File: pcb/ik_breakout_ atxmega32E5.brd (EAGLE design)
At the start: 41.3 x 20.3 mm, 31 parts, among them IC1 FT230XS, J1 AVR_SPI_PRG_62X3_LOCK, U1 MIC5219 3.3V

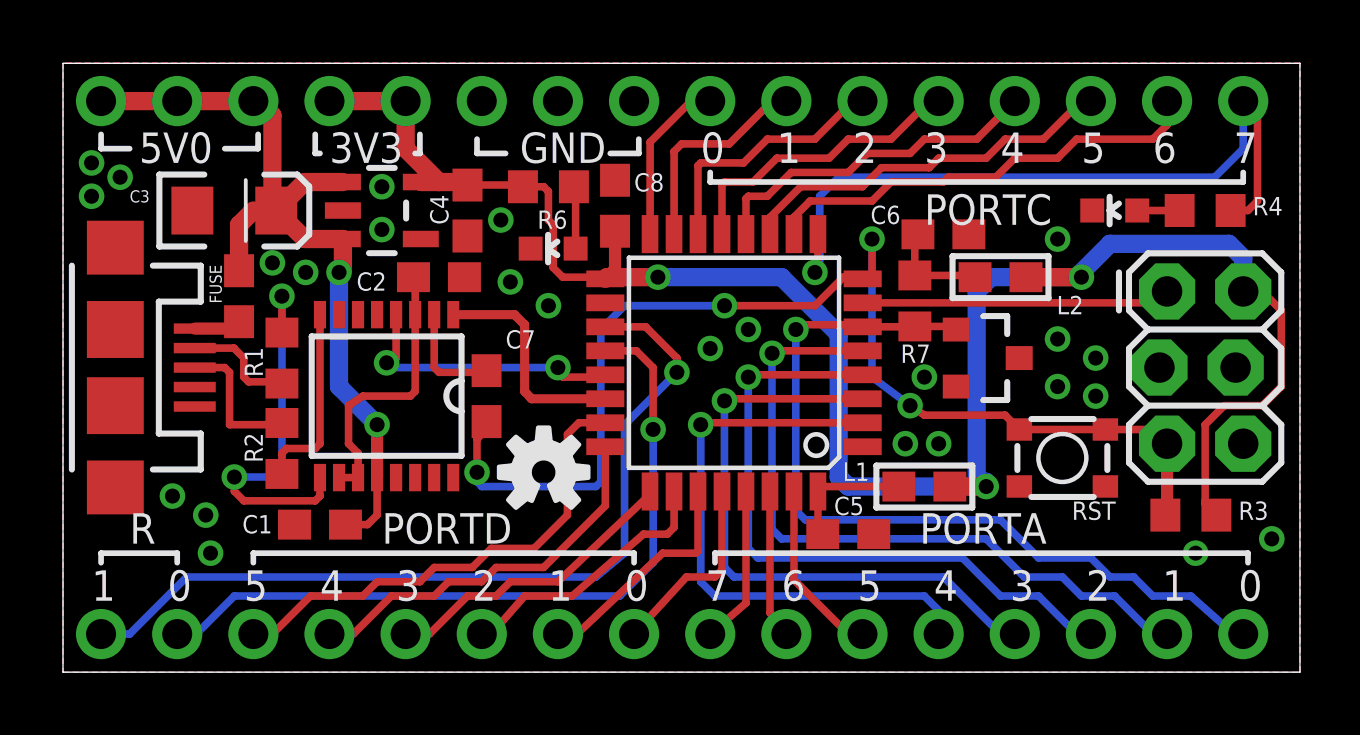
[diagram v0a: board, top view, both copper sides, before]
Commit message: oops. committed from /pcb/fab/gerbers folder.
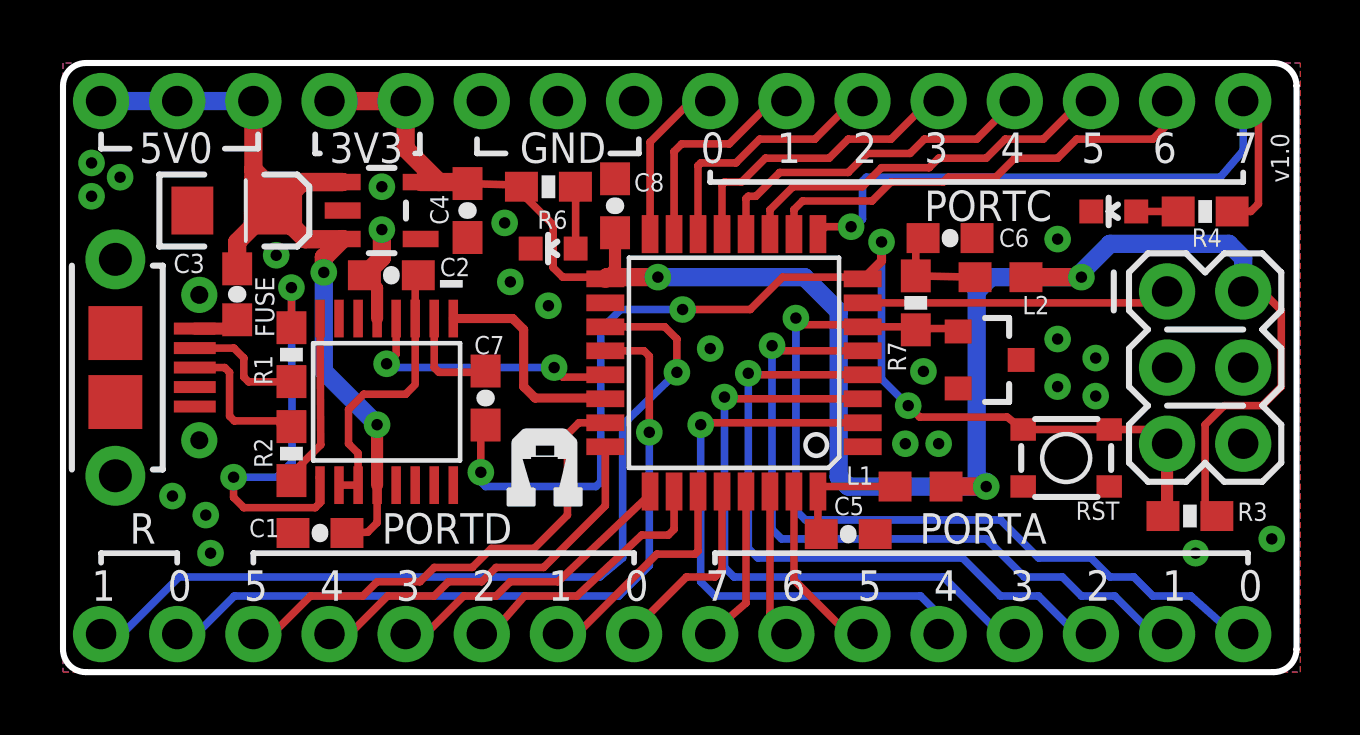
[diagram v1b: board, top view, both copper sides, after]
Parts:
- removed JP6, JP7, JP8, JP9: (no value), microbuilder:1X08_ROUND
- removed LED3: (no value), SparkFun-LED:LED-0603
- removed U$1: IHSAN_XMEGA_E5, SparkFun-DigitalIC_ihsan:TQFP32-08
- removed U$2: IHSAN_LM4040, SparkFun-DigitalIC_ihsan:SOT23-3
- added IC2: ATXMEGA32E5, Ai_IC:TQFP32-08
- added JP1, JP2, JP3, JP4: 1X08NOFIRST, Ai_Connectors:1X08-NOFIRST
- added LED1: (no value), Ai_LED:LED-0603
- added U$3: AI-LOGOXS, Ai_Miscellany:AI-LOGO-XS
- added U2: IHSAN_LM4040, SparkFun-DigitalIC_ihsan:SOT23-3
- C1, C2, C5, C6, C7: value .1 -> 0.1uF; device rcl:C0603 -> Ai_Passives:CAP-0603
- C3: device SparkFun-Capacitors:EIA3216 -> Ai_Passives:CAP-POL-EIA3216
- C4, C8: value 4.7 uF -> 4.7uF; device rcl:C0603 -> Ai_Passives:CAP-0603
- FUSE: device SparkFun-Passives:0603 -> Ai_Passives:FB-0603
- IC1: value FT230XS -> FT230X; device ftdichip:SSOP16 -> Ai_IC:SSOP-16-FTDI
- J1: value AVR_SPI_PRG_62X3_LOCK -> 2X03; device SparkFun-Connectors:2X3_LOCK -> Ai_Connectors:2X03
- L1, L2: device microbuilder:0603 -> Ai_Passives:IND-0603
- LED2: device SparkFun-LED:LED-0603 -> Ai_LED:LED-0603
- R1, R2, R3, R4, R6, R7: device rcl:R0603 -> Ai_Passives:RES-0603
- U1: value MIC5219 3.3V -> MIC5219-3.3; device SparkFun-PowerIC:SOT23-5 -> Ai_Power:SOT23-5
- USB1: value USBMICROB-SMD -> USBMICROB-TH; device Ai_Connectors:USB-MICROB-SMD -> Ai_Connectors:USB-MICROB-TH
- moved LOGO1 9.09 mm to (22.4, 13.2), flipped to the bottom
- moved J1 2.84 mm to (38.1, 10.2)
- moved C2 1.59 mm to (11.0, 13.2), turned to 180 degrees
- moved R2 0.36 mm to (7.62, 7.29)
- moved R1 0.34 mm to (7.62, 10.6)
- moved C1 0.28 mm to (8.57, 4.64)
- moved C6 0.26 mm to (29.6, 14.5)
- moved IC1 0.19 mm to (10.8, 9.02), turned to 180 degrees
- moved RST 0.13 mm to (33.5, 7.14)
- moved L1 0.13 mm to (28.6, 6.19)
- moved FUSE 0.09 mm to (5.81, 12.6), turned to 90 degrees
- moved C7 0.07 mm to (14.1, 9.14)
- moved R7 0.07 mm to (28.4, 12.3)
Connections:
- net /RTS renamed !RTS
- removed net 5V0: C1.1, C3.A, FUSE.1, IC1.12, JP9.1, JP9.2, JP9.3, U1.1, U1.3
- removed net N$10: FUSE.2, USB1.VBUS
- new net 5V: C1.1, C3.A, FUSE.2, IC1.12, JP4.1, JP4.2, JP4.3, U1.1, U1.3
- new net VBUS: FUSE.1, USB1.VBUS
- net 3V3: now also IC2.17, JP4.4, JP4.5; no longer JP9.4, JP9.5, U$1.17
- net AVCC: now also IC2.32; no longer U$1.32
- net FT_RX: now also IC2.21; no longer U$1.21
- net FT_TX: now also IC2.22; no longer U$1.22
- net GND: now also IC2.1, IC2.18, JP4.6, JP4.7, JP4.8, LED1.C, U2.2; no longer JP9.6, JP9.7, JP9.8, LED3.C, U$1.1, U$1.18, U$2.2
- net N$8: now also LED1.A; no longer LED3.A
- net PA0: now also IC2.6, JP2.1, U2.1; no longer JP8.1, U$1.6, U$2.1
- net PA1: now also IC2.5, JP2.2; no longer JP8.2, U$1.5
- net PA2: now also IC2.4, JP2.3; no longer JP8.3, U$1.4
- net PA3: now also IC2.3, JP2.4; no longer JP8.4, U$1.3
- net PA4: now also IC2.2, JP2.5; no longer JP8.5, U$1.2
- net PA5: now also IC2.31, JP2.6; no longer JP8.6, U$1.31
- net PA6: now also IC2.30, JP2.7; no longer JP8.7, U$1.30
- net PA7: now also IC2.29, JP2.8; no longer JP8.8, U$1.29
- net PC0: now also IC2.16, JP3.1; no longer JP6.1, U$1.16
- net PC1: now also IC2.15, JP3.2; no longer JP6.2, U$1.15
- net PC2: now also IC2.14, JP3.3; no longer JP6.3, U$1.14
- net PC3: now also IC2.13, JP3.4; no longer JP6.4, U$1.13
- net PC4: now also IC2.12, JP3.5; no longer JP6.5, U$1.12
- net PC5: now also IC2.11, JP3.6; no longer JP6.6, U$1.11
- net PC6: now also IC2.10, JP3.7; no longer JP6.7, U$1.10
- net PC7: now also IC2.9, JP3.8; no longer JP6.8, U$1.9
- net PD0: now also IC2.28, JP1.1; no longer JP7.1, U$1.28
- net PD1: now also IC2.27, JP1.2; no longer JP7.2, U$1.27
- net PD2: now also IC2.26, JP1.3; no longer JP7.3, U$1.26
- net PD3: now also IC2.25, JP1.4; no longer JP7.4, U$1.25
- net PD4: now also IC2.24, JP1.5; no longer JP7.5, U$1.24
- net PD5: now also IC2.23, JP1.6; no longer JP7.6, U$1.23
- net PDI_C: now also IC2.8; no longer U$1.8
- net PDI_D: now also IC2.7; no longer U$1.7
- net PR0: now also IC2.20, JP1.7; no longer JP7.7, U$1.20
- net PR1: now also IC2.19, JP1.8; no longer JP7.8, U$1.19
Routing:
- net 5V: track 0.00 -> 31.2 mm, vias 0 -> 2
- net 5V0: track 28.3 -> 0.00 mm, vias 2 -> 0
- net GND: track 0.00 -> 3.38 mm, vias 25 -> 23
- net PC7: track 24.9 -> 22.4 mm
- net N$10: track 1.65 -> 0.00 mm
- net VBUS: track 0.00 -> 1.54 mm
- net D-: track 12.9 -> 13.9 mm
- net PDI_C: track 40.4 -> 39.7 mm
- net D+: track 6.40 -> 5.81 mm
- net PA0: track 28.1 -> 28.7 mm
- net N$2: track 4.74 -> 5.27 mm
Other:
- board size 41.3 x 20.3 mm -> 41.1 x 20.3 mm
- board text added: "ATxmega32E5"
- board text added: "Ihsan Kehribar"
- board text added: "v1.0"
- board text added: "www.acrobotic.com"
- board text removed: "<ihsan@kehribar.me> - 2014"
- board text removed: "Xmega E5"
- board text removed: "v0.4"

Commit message: changed LM4040 to include part on Ai_Power library
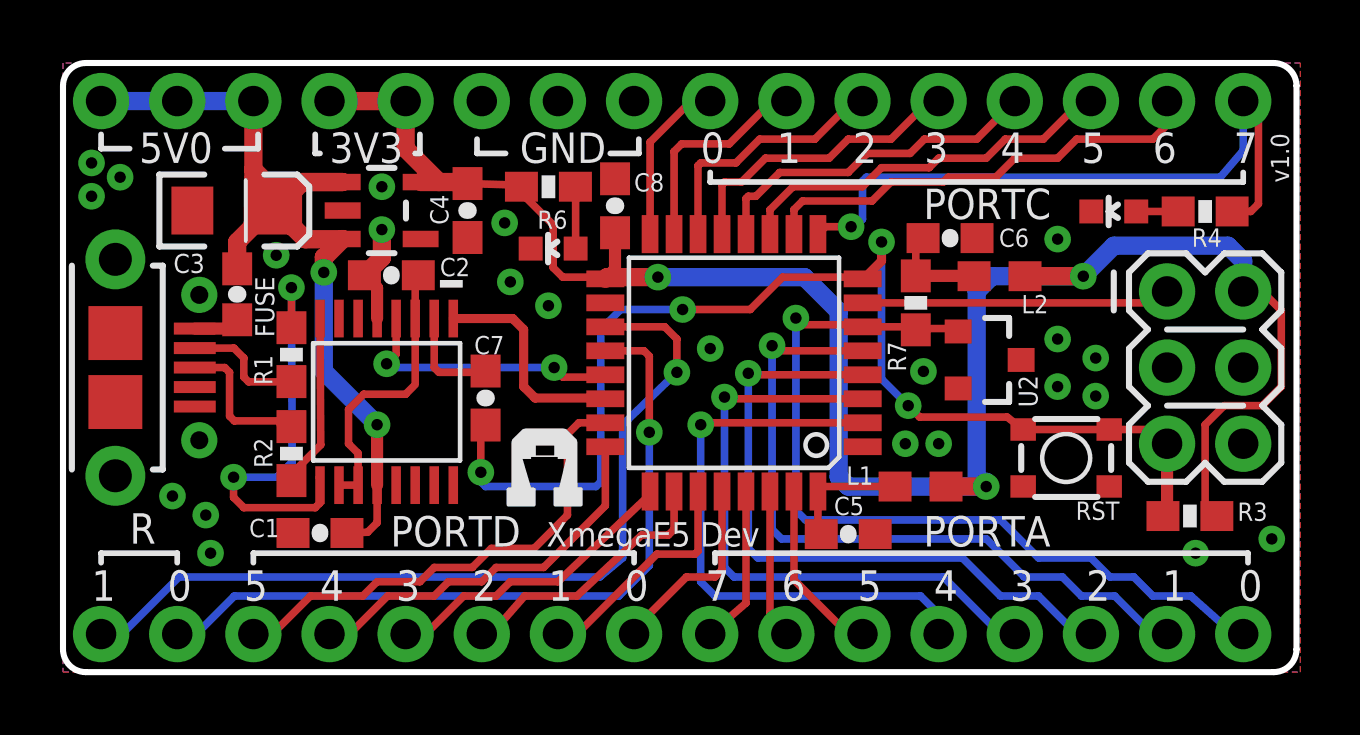
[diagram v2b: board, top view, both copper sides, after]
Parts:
- U2: value IHSAN_LM4040 -> LM4040; device SparkFun-DigitalIC_ihsan:SOT23-3 -> Ai_Power:SOT23-3
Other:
- board text added: "XmegaE5 Dev"
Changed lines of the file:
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@@
 <setting verticaltext="up"/>
 </settings>
-<grid distance="10" unitdist="mil" unit="mil" style="lines" multiple="1" display="yes" altdistance="0.025" altunitdist="inch" altunit="inch"/>
+<grid distance="5" unitdist="mil" unit="mil" style="lines" multiple="1" display="yes" altdistance="0.025" altunitdist="inch" altunit="inch"/>
 <layers>
 <layer number="1" name="Top" color="4" fill="1" visible="yes" active="yes"/>
@@
 <layer number="45" name="Holes" color="7" fill="1" visible="no" active="yes"/>
 <layer number="46" name="Milling" color="3" fill="1" visible="no" active="yes"/>
-<layer number="47" name="Measures" color="7" fill="1" visible="no" active="yes"/>
-<layer number="48" name="Document" color="7" fill="1" visible="no" active="yes"/>
-<layer number="49" name="Reference" color="7" fill="1" visible="no" active="yes"/>
+<layer number="47" name="Measures" color="7" fill="1" visible="yes" active="yes"/>
+<layer number="48" name="Document" color="7" fill="1" visible="yes" active="yes"/>
+<layer number="49" name="Reference" color="7" fill="1" visible="yes" active="yes"/>
 <layer number="50" name="dxf" color="7" fill="1" visible="no" active="no"/>
 <layer number="51" name="tDocu" color="7" fill="1" visible="no" active="yes"/>
@@
 <text x="16.1925" y="2.38125" size="1.016" layer="21" font="vector" ratio="15">1</text>
 <text x="18.7325" y="2.38125" size="1.016" layer="21" font="vector" ratio="15">0</text>
-<text x="10.63625" y="4.28625" size="1.016" layer="21" font="vector" ratio="15">PORTD</text>
+<text x="10.922" y="4.191" size="1.016" layer="21" font="vector" ratio="15">PORTD</text>
 <wire x1="21.74875" y1="3.65125" x2="21.74875" y2="3.96875" width="0.1905" layer="21"/>
 <wire x1="21.74875" y1="3.96875" x2="39.52875" y2="3.96875" width="0.1905" layer="21"/>
@@
 <text x="36.67125" y="2.38125" size="1.016" layer="21" font="vector" ratio="15">1</text>
 <text x="39.21125" y="2.38125" size="1.016" layer="21" font="vector" ratio="15">0</text>
-<text x="28.575" y="4.28625" size="1.016" layer="21" font="vector" ratio="15">PORTA</text>
+<text x="28.702" y="4.191" size="1.016" layer="21" font="vector" ratio="15">PORTA</text>
 <wire x1="39.37" y1="16.66875" x2="39.37" y2="16.35125" width="0.1905" layer="21"/>
 <wire x1="39.37" y1="16.35125" x2="21.59" y2="16.35125" width="0.1905" layer="21"/>
@@
 <text x="23.8125" y="16.98625" size="1.016" layer="21" font="vector" ratio="15">1</text>
 <text x="21.2725" y="16.98625" size="1.016" layer="21" font="vector" ratio="15">0</text>
-<text x="28.73375" y="15.0495" size="1.016" layer="21" font="vector" ratio="15">PORTC</text>
+<text x="28.702" y="15.113" size="1.016" layer="21" font="vector" ratio="15">PORTC</text>
 <text x="2.54" y="16.98625" size="1.016" layer="21" font="vector" ratio="15">5V0</text>
 <text x="8.89" y="16.98625" size="1.016" layer="21" font="vector" ratio="15">3V3</text>
@@
 <text x="14.224" y="5.55625" size="1.016" layer="22" font="vector" ratio="15" rot="MR180">www.acrobotic.com</text>
 <text x="40.90035" y="16.3322" size="0.6096" layer="21" font="vector" ratio="15" rot="R90">v1.0</text>
+<text x="16.129" y="4.191" size="0.8128" layer="21" font="vector" ratio="15">XmegaE5 Dev</text>
 </plain>
 <attributes>
@@
 <attribute name="VALUE" x="26.57475" y="6.95325" size="0.4064" layer="27" ratio="10" rot="R180"/>
 </element>
-<element name="L2" library="Ai_Passives" package="IND-0603" value="" x="31.27375" y="13.17625" smashed="yes">
-<attribute name="NAME" x="32.004" y="11.938" size="0.6096" layer="25" font="vector" ratio="15"/>
-<attribute name="VALUE" x="33.30575" y="12.41425" size="0.4064" layer="27" ratio="10"/>
+<element name="L2" library="Ai_Passives" package="IND-0603" value="" x="31.242" y="13.208" smashed="yes">
+<attribute name="NAME" x="31.97225" y="11.96975" size="0.6096" layer="25" font="vector" ratio="15"/>
+<attribute name="VALUE" x="33.274" y="12.446" size="0.4064" layer="27" ratio="10"/>
 </element>
 <element name="R3" library="Ai_Passives" package="RES-0603" value="" x="37.592" y="5.207" smashed="yes">
@@
 <attribute name="NAME" x="32.22625" y="14.7955" size="0.6096" layer="25" font="vector" ratio="15" rot="R180"/>
 </element>
-<element name="U2" library="SparkFun-DigitalIC_ihsan" package="SOT23-3" value="IHSAN_LM4040" x="30.861" y="10.414" smashed="yes" rot="R270"/>
+<element name="U2" library="Ai_Power" package="SOT23-3" value="LM4040" x="30.861" y="10.414" smashed="yes" rot="R270">
+<attribute name="NAME" x="31.877" y="9.906" size="0.635" layer="21" font="vector" ratio="15" rot="R270"/>
+</element>
 <element name="FUSE" library="Ai_Passives" package="FB-0603" value="FB" x="5.81025" y="12.60475" smashed="yes" rot="R90">
 <attribute name="NAME" x="7.0485" y="11.176" size="0.635" layer="25" font="vector" ratio="15" rot="R90"/>
@@
 <wire x1="30.63875" y1="6.19125" x2="30.48" y2="6.35" width="0.6096" layer="16"/>
 <wire x1="30.48" y1="6.35" x2="30.48" y2="12.7" width="0.6096" layer="16"/>
-<wire x1="30.48" y1="12.7" x2="30.95625" y2="13.17625" width="0.6096" layer="16"/>
-<via x="33.9725" y="13.17625" extent="1-16" drill="0.381"/>
-<wire x1="33.81375" y1="13.17625" x2="33.9725" y2="13.17625" width="0.6096" layer="16"/>
-<wire x1="33.9725" y1="13.17625" x2="32.12375" y2="13.17625" width="0.6096" layer="1"/>
-<wire x1="30.95625" y1="13.17625" x2="33.81375" y2="13.17625" width="0.6096" layer="16"/>
-<wire x1="33.81375" y1="13.17625" x2="34.925" y2="14.2875" width="0.6096" layer="16"/>
-<wire x1="34.925" y1="14.2875" x2="38.89375" y2="14.2875" width="0.6096" layer="16"/>
-<wire x1="38.89375" y1="14.2875" x2="39.37" y2="13.81125" width="0.6096" layer="16"/>
-<wire x1="39.37" y1="13.81125" x2="39.37" y2="12.7" width="0.6096" layer="16"/>
+<wire x1="30.48" y1="12.7" x2="30.988" y2="13.208" width="0.6096" layer="16"/>
+<via x="34.036" y="13.208" extent="1-16" drill="0.381"/>
+<wire x1="34.036" y1="13.208" x2="32.092" y2="13.208" width="0.6096" layer="1"/>
+<wire x1="30.988" y1="13.208" x2="34.036" y2="13.208" width="0.6096" layer="16"/>
+<wire x1="34.036" y1="13.208" x2="35.052" y2="14.224" width="0.6096" layer="16"/>
+<wire x1="35.052" y1="14.224" x2="38.862" y2="14.224" width="0.6096" layer="16"/>
+<wire x1="38.862" y1="14.224" x2="39.37" y2="13.716" width="0.6096" layer="16"/>
+<wire x1="39.37" y1="13.716" x2="39.37" y2="12.7" width="0.6096" layer="16"/>
 <wire x1="15.2925" y1="16.1925" x2="15.29625" y2="16.24875" width="0.254" layer="1"/>
 <wire x1="13.49375" y1="16.29875" x2="15.15925" y2="16.24875" width="0.254" layer="1"/>
@@
 <contactref element="L2" pad="1"/>
 <contactref element="C6" pad="1"/>
-<wire x1="30.42375" y1="13.17625" x2="30.42285" y2="13.17535" width="0.254" layer="1"/>
-<wire x1="30.42285" y1="13.17535" x2="28.448" y2="13.219" width="0.254" layer="1"/>
 <wire x1="28.448" y1="13.219" x2="28.448" y2="14.185" width="0.254" layer="1"/>
 <wire x1="28.448" y1="14.185" x2="28.691" y2="14.478" width="0.254" layer="1"/>
+<wire x1="28.448" y1="13.219" x2="30.381" y2="13.219" width="0.4064" layer="1"/>
+<wire x1="30.381" y1="13.219" x2="30.392" y2="13.208" width="0.4064" layer="1"/>
 </signal>
 <signal name="!RTS">
